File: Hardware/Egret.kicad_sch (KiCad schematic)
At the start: 0 parts

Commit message: update schematic.
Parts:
- added C? (x2): C, symbol Device:C
- added D? (x3): LESD5D5.0CT1G, TVS_LESD5D5.0CT1G, symbol LESD5D5.0CT1G:LESD5D5.0CT1G
- added D?: LED, symbol Device:LED
- added D?: BAT760, SOD323(F), symbol BAT760:BAT760
- added J?: USB_B_Micro, symbol Connector:USB_B_Micro
- added Q? (x2): S8050, Package_TO_SOT_THT:TO-92_Inline, symbol Transistor_BJT:S8050
- added R? (x7): R, symbol Device:R
- added U?: ESP32-PICO-D4, Package_DFN_QFN:QFN-48-1EP_7x7mm_P0.5mm_EP5.3x5.3mm, symbol RF_Module:ESP32-PICO-D4
- added U?: AMS1117-3.3, Package_TO_SOT_SMD:SOT-223-3_TabPin2, symbol Regulator_Linear:AMS1117-3.3
- added U?: CP2102N-Axx-xQFN28, Package_DFN_QFN:QFN-28-1EP_5x5mm_P0.5mm_EP3.35x3.35mm, symbol Interface_USB:CP2102N-Axx-xQFN28
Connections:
- new net: D?.2, J?.2 (D-), R?.1
- new net: U?.1 (VDDA), U?.43 (VDDA), U?.46 (VDDA)
- new net: U?.3 (VDDA3P3), U?.4 (VDDA3P3)
- new net: C?.1, U?.2 (VO)
- new net: D?.2, D?.2, D?.2, J?.1 (VBUS), J?.3 (D+), R?.1
- new net: D?.2 (A), R?.2
- new net: C?.1, R?.1, U?.3 (VI)
- new net: U?.29 (GND), U?.3 (GND)
- new net EXT_5V: D?.1
- new net GND: C?.2, C?.2, D?.1, D?.1, D?.1, D?.1 (K), J?.5 (GND), J?.6 (Shield), U?.1 (GND)
- new net USB_DN: R?.2
- new net USB_DP: R?.2
- no-connect marks 0 -> 1
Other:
- note added: "电源"
- company: (none) -> www.UinIO.com
- title: (none) -> Egret

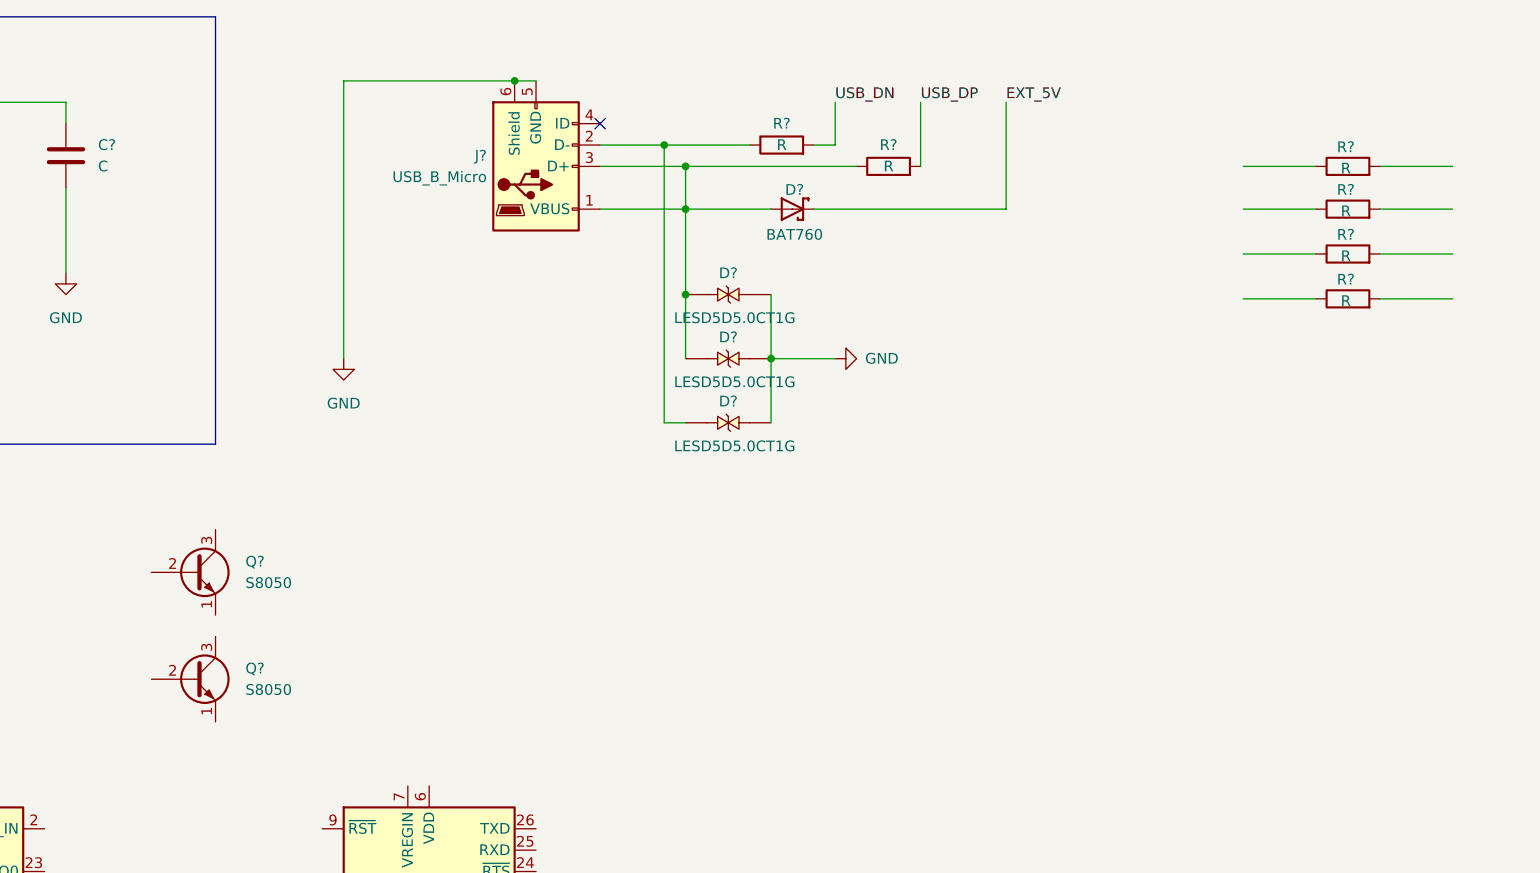
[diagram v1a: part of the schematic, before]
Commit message: update schematic.
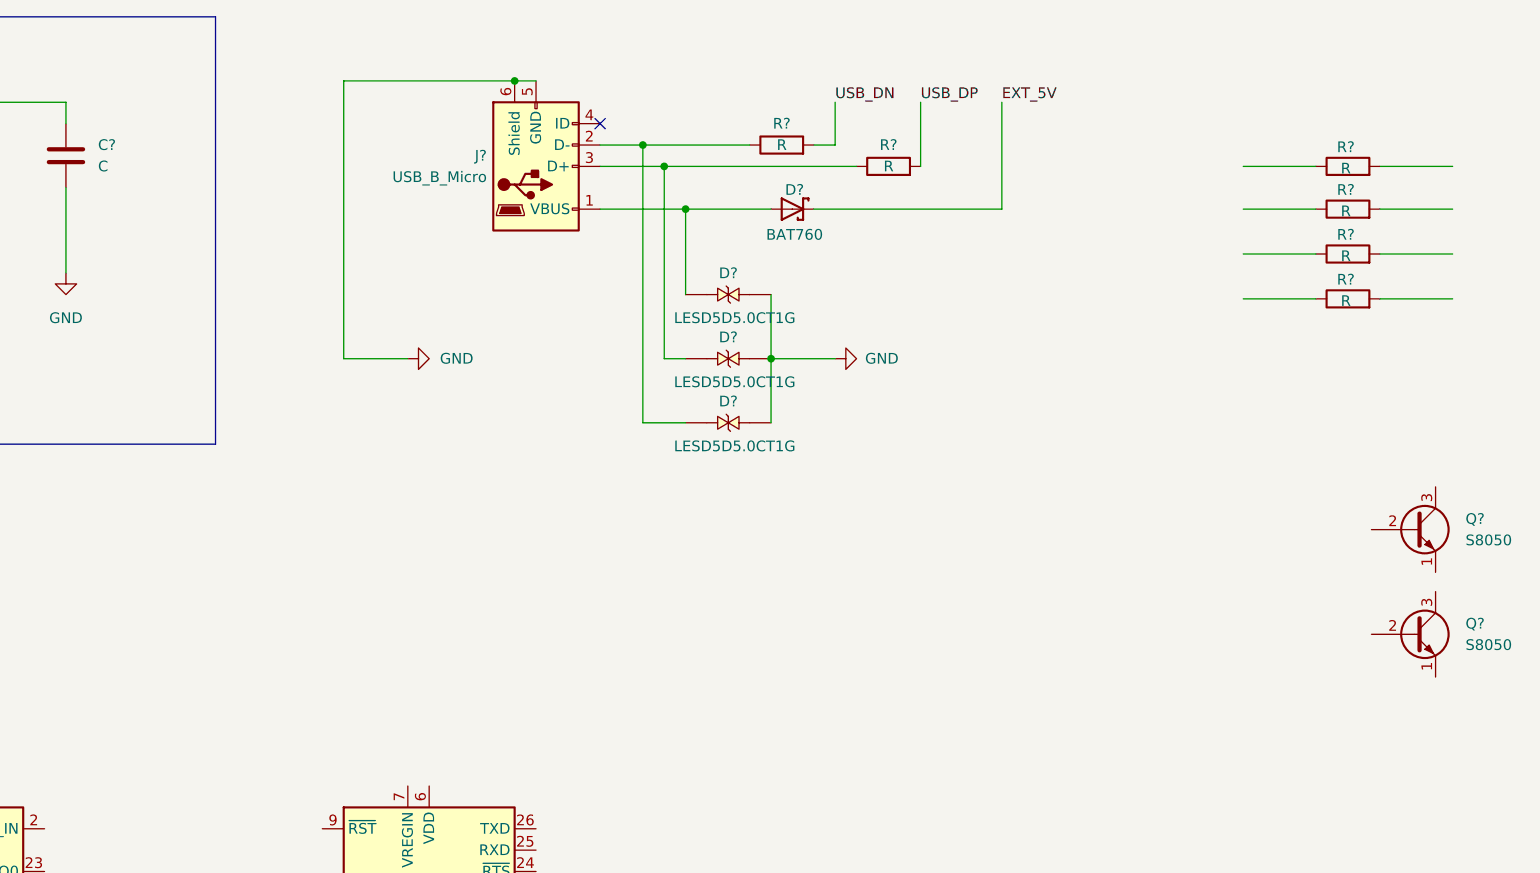
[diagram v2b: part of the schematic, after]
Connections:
- net at D?.2, J?.3 (D+), R?.1: no longer D?.2, D?.2, J?.1 (VBUS)
- new net: D?.2, D?.2, J?.1 (VBUS)
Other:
- moved on the sheet: Q?

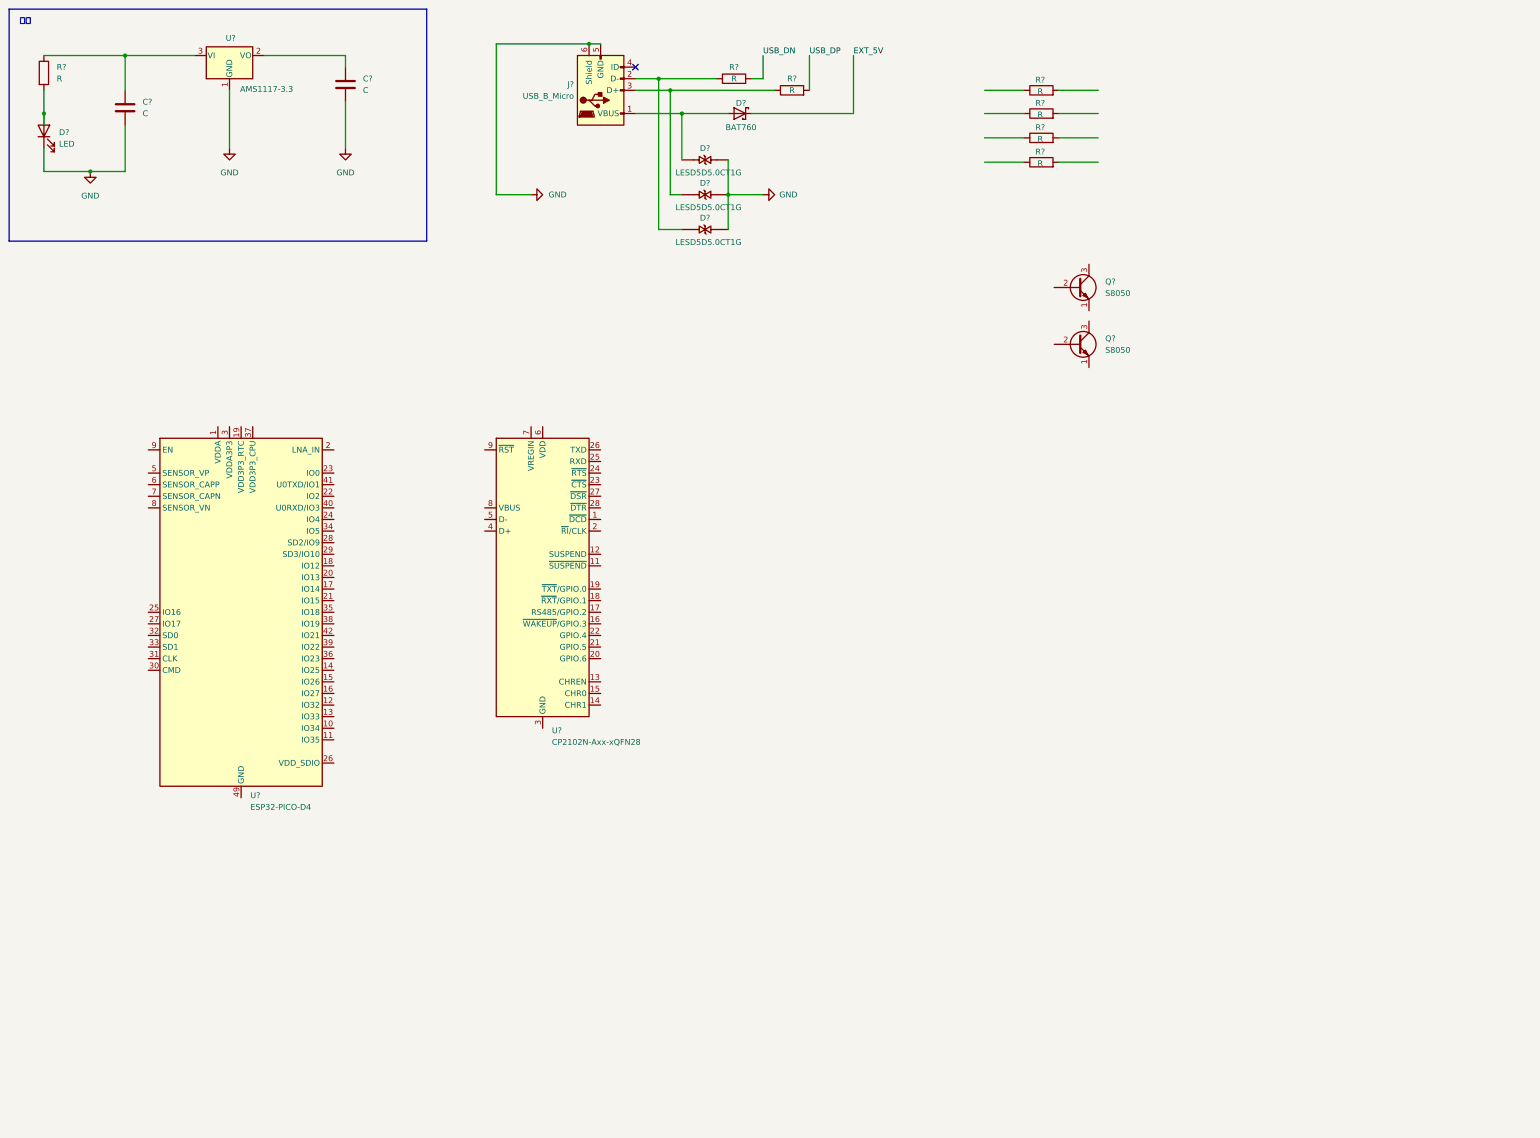
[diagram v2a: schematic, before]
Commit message: add additional libraries.
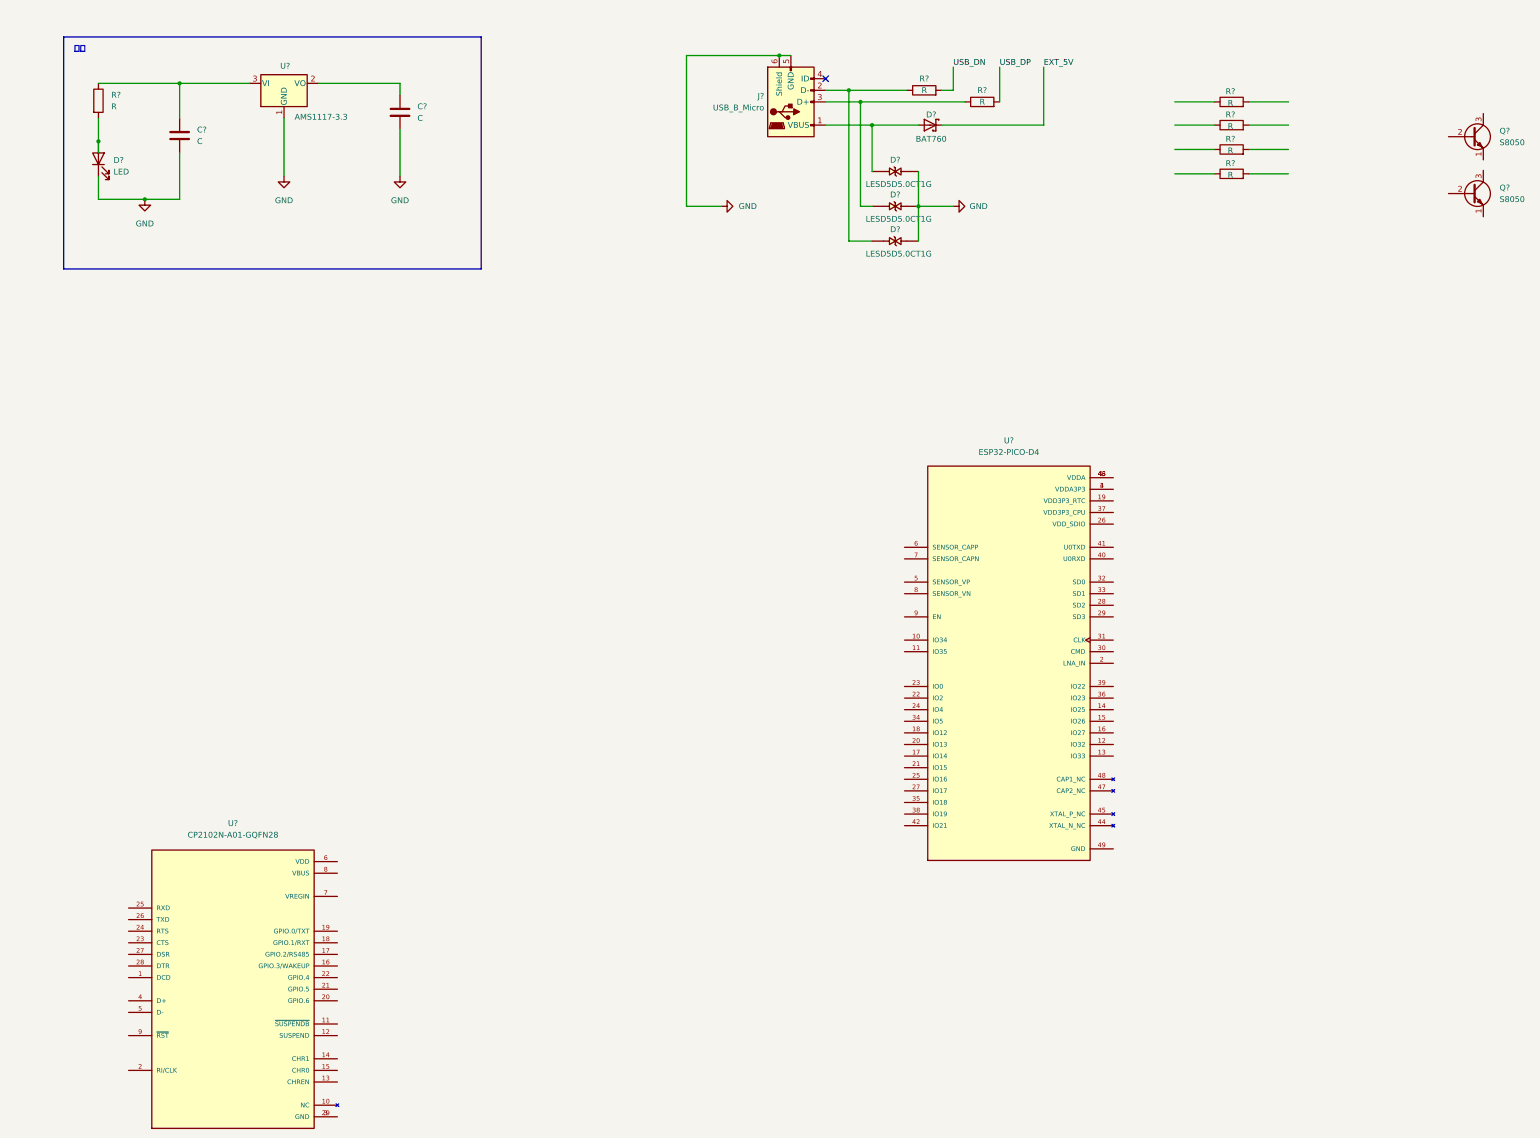
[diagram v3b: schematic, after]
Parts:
- removed U?: ESP32-PICO-D4, Package_DFN_QFN:QFN-48-1EP_7x7mm_P0.5mm_EP5.3x5.3mm, symbol RF_Module:ESP32-PICO-D4
- removed U?: CP2102N-Axx-xQFN28, Package_DFN_QFN:QFN-28-1EP_5x5mm_P0.5mm_EP3.35x3.35mm, symbol Interface_USB:CP2102N-Axx-xQFN28
- added U?: CP2102N-A01-GQFN28, QFN50P500X500X80-29N, symbol CP2102N-A01-GQFN28:CP2102N-A01-GQFN28
- added U?: ESP32-PICO-D4, PQFN50P700X700X104-49N, symbol ESP32-PICO-D4:ESP32-PICO-D4
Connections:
- new net: U?.29 (GND), U?.3 (GND)
- new net: U?.1 (VDDA), U?.43 (VDDA), U?.46 (VDDA)
- new net: U?.3 (VDDA3P3), U?.4 (VDDA3P3)
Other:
- moved on the sheet: C?, D?, J?, Q?, R?, U?

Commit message: update
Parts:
- removed R? (x3): R, symbol Device:R
- added C?: 0.1uF/25V(10%), symbol Device:C
- added J? (x2): Conn_01x20_Male, symbol Connector:Conn_01x20_Male
- added R? (x2): 10K (1%), symbol Device:R
- added R? (x2): 0R(1%)(NC), symbol Device:R
- added R?: 22.1K(1%), symbol Device:R
- added R?: 2K (1%), symbol Device:R
- added R?: 1K(1%), symbol Device:R
- added R?: 47.5K(1%), symbol Device:R
- added R?: 10K(1%)(NC), symbol Device:R
- C?: value C -> 10uF/25V (10%)
- C?: value C -> 10uF/25V(10%)
- D?: value LED -> Red LED
- R?: value R -> 0R (1%)
- R?: value R -> 1K(1%)
- R?: value R -> 2k (1%)
- R?: value R -> 0R(1%)
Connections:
- net GND: now also U?.29 (GND), U?.3 (GND), U?.49 (GND), C?.2, R?.2, R?.2
- net USB_DN: now also U?.5 (D-)
- net USB_DP: now also U?.4 (D+)
- net VDD33: now reaches C?.1, U?.2 (VO)
- net VDD33: now also R?.2
- net TXD0: now reaches R?.1
- net RXD: now reaches R?.2
- net RXD: now also U?.25 (RXD)
- net at U?.11 (~{SUSPENDB}): now also R?.1
- net CTS: now reaches U?.23 (CTS)
- net CTS: now also R?.2
- net RTS: now reaches U?.24 (RTS)
- net RTS: now also Q?.1 (E), R?.2, R?.2
- net TXD: now reaches U?.26 (TXD)
- net TXD: now also R?.2
- net DTR: now reaches U?.28 (DTR)
- net DTR: now also Q?.1 (E), R?.2
- net at U?.6 (VDD): now also U?.7 (VREGIN), C?.1
- net at U?.8 (VBUS): now also R?.1, R?.2
- net at U?.9 (~{RST}): now also R?.1
- net at Q?.2 (B): now also R?.1 (x2)
- net EN: now reaches Q?.3 (C)
- net IO0: now reaches Q?.3 (C)
- net VDD33A: now reaches U?.1 (VDDA), U?.43 (VDDA), U?.46 (VDDA)
- net FLASH_CS: now reaches U?.25 (IO16)
- net FLASH_SD0: now reaches U?.27 (IO17)
- net IO9: now reaches U?.28 (SD2)
- net IO10: now reaches U?.29 (SD3)
- net FLASH_SD2: now reaches U?.30 (CMD)
- net FLASH_CLK: now reaches U?.31 (CLK)
- net FLASH_SD3: now reaches U?.32 (SD0)
- net FLASH_SD1: now reaches U?.33 (SD1)
- net IO5: now reaches U?.34 (IO5)
- net IO18: now reaches U?.35 (IO18)
- net IO23: now reaches U?.36 (IO23)
- new net IO13: R?.1
- new net IO15: R?.1
- new net RXD0: R?.1
- no-connect marks 1 -> 15
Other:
- note added: "Auto program DTR RTS-->EN IO0 1 1 1 1 0 0 1 1 1 0 0 1 0 1 1 0"
- note added: "USB与串口"
- moved on the sheet: C?, D?, J?, Q?, R?, U?
